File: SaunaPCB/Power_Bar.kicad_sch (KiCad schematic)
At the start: 58 parts, among them J201 KL3RM7.62, J202 KL3RM7.62, J203 KL3RM7.62, J204 KL2RM5.08, J205 KL3RM7.62, J206 KL3RM7.62, K201 RP310024, K202 RP310024, K203 RP310024, K204 RP310024, K205 RP310024, K206 RP310024, K207 RP310024, U201 LHE05-20B24, U202 LM2576T-5, U203 4N25, U204 4N25, U205 4N25, U206 DRV5053, U207 DRV5053, U208 DRV5053

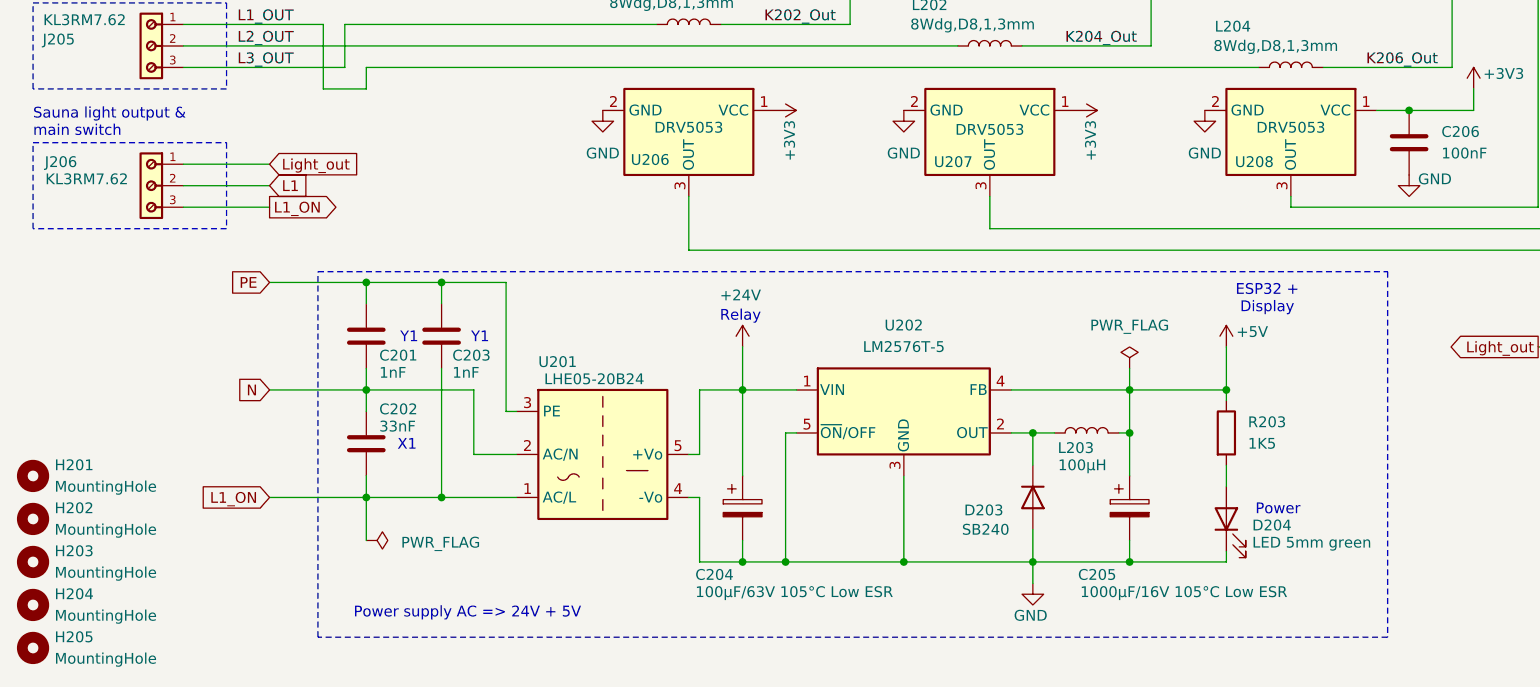
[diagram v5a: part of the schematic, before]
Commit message: ^MOV and Fuse added
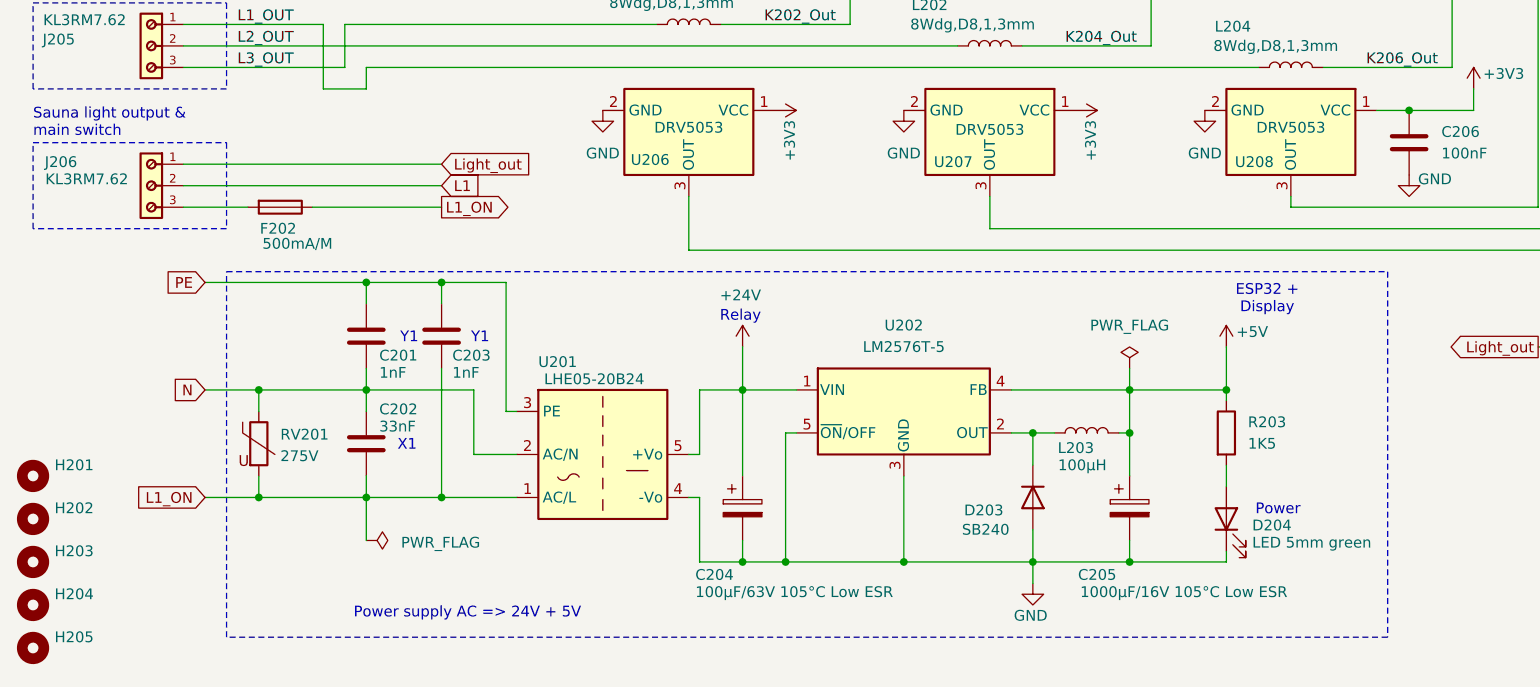
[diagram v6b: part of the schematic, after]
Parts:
- added F202: 500mA/M, Fuse:Fuseholder_Cylinder-5x20mm_Schurter_0031_8201_Horizontal_Open, symbol Device:Fuse
- added RV201: 275V, Varistor:RV_Disc_D12mm_W4.2mm_P7.5mm, symbol Device:Varistor
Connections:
- net L1_ON: now also F202.1, RV201.2; no longer J206.3
- net N: now also RV201.1
- new net: F202.2, J206.3

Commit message: Power LED changed to JST connector KTY room added
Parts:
- D204: footprint Connector_JST:JST_EH_B2B-EH-A_1x02_P2.50mm_Vertical -> MyConnectors:B2B-ZR
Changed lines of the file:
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@@
 			)
 		)
-		(property "Footprint" "Connector_JST:JST_EH_B2B-EH-A_1x02_P2.50mm_Vertical"
+		(property "Footprint" "MyConnectors:B2B-ZR"
 			(at 156.21 177.8 0)
 			(effects

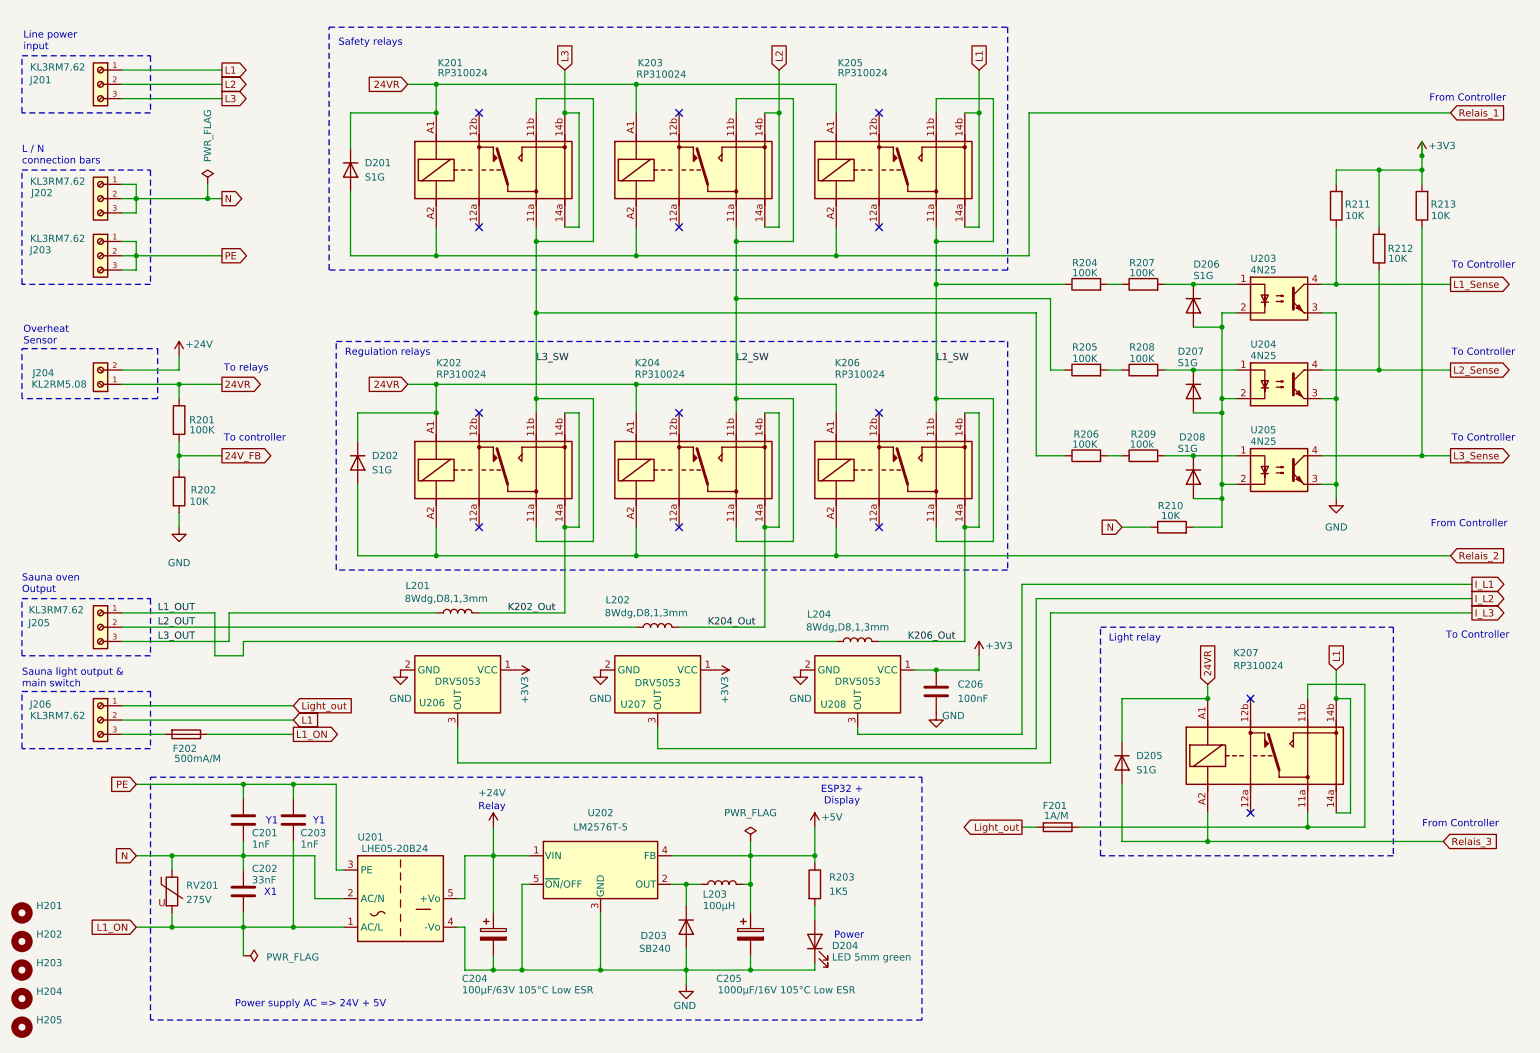
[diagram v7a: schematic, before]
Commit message: Home brew sensor: Coil and hall sensor combined to one unit to avoid overlap errors on DRC DRC errors removed; 2 warnings left => both acceptable.
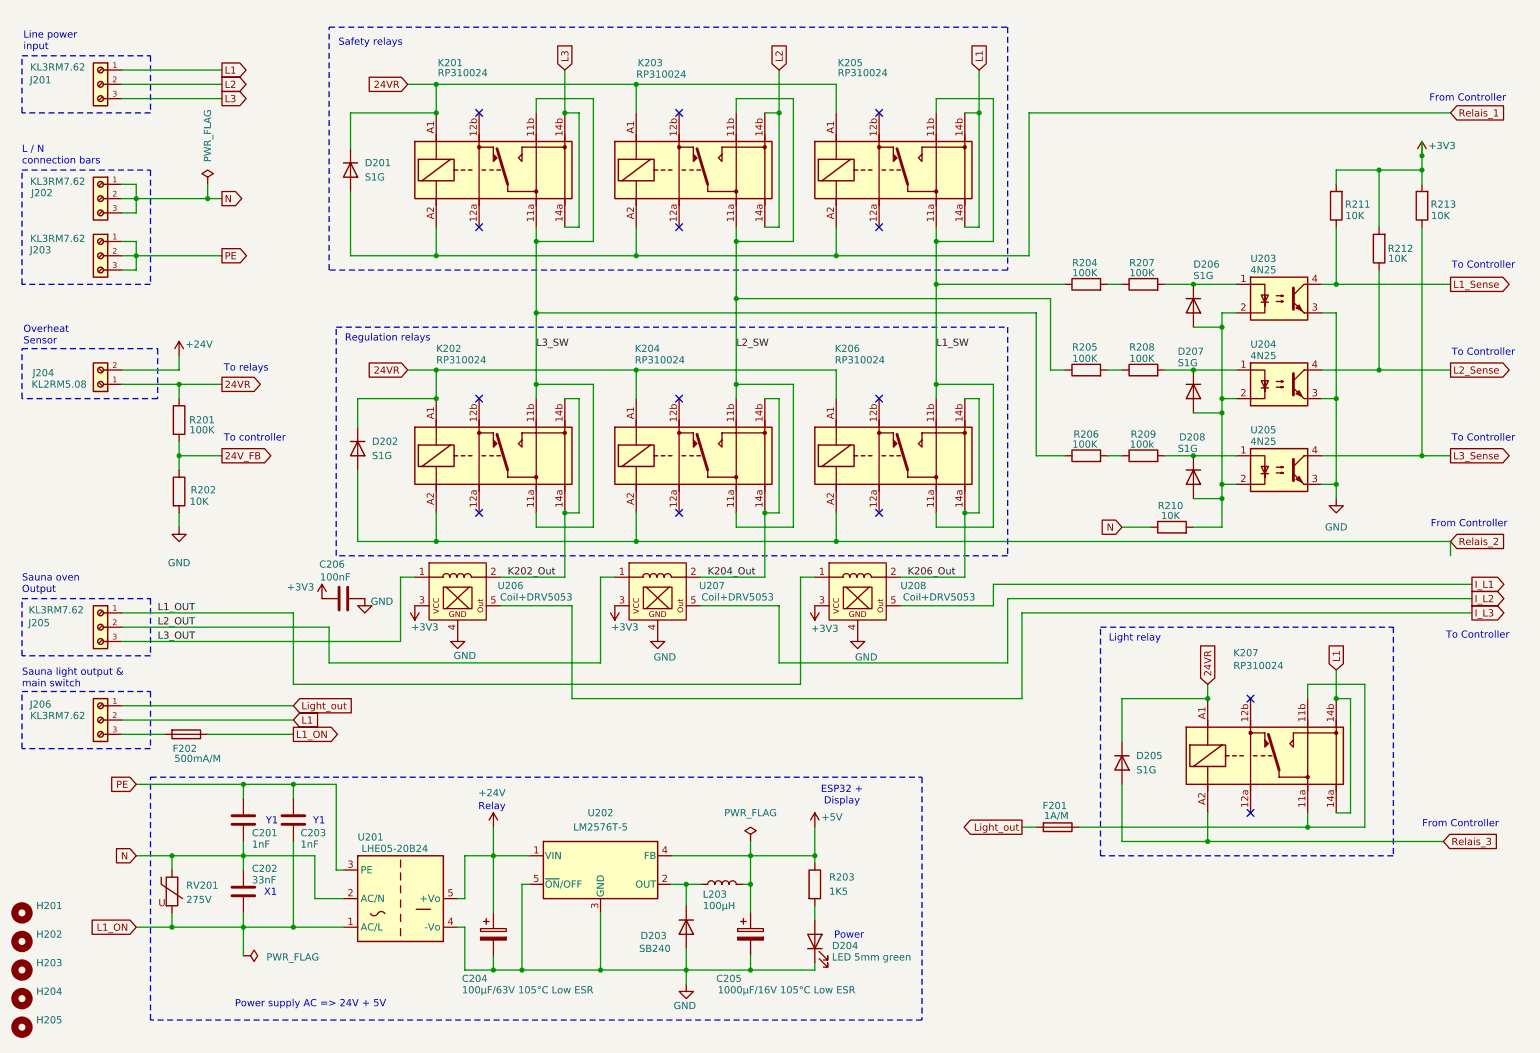
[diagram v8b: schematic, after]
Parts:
- removed L201, L202, L204: 8Wdg,D8,1,3mm, SaunaProject:Current_Coil_19X14, symbol Device:L
- removed U206, U207, U208: DRV5053, Package_TO_SOT_THT:TO-92_Inline, symbol Sensor_Magnetic:DRV5033AJxLPG
- added U206, U207, U208: Coil+DRV5053, SaunaProject:Current_Coil_19X14_w_Hall, symbol Project:HomeBrewISens
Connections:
- net +3V3: now also U206.3, U207.3, U208.3
- net GND: now also U206.4, U207.4, U208.4
- net I_L1: now also U208.5
- net I_L2: now also U207.5
- net I_L3: now also U206.5
- net K202_Out: now also U206.2
- net K204_Out: now also U207.2
- net K206_Out: now also U208.2
- net L1_OUT: now also U208.1
- net L2_OUT: now also U207.1
- net L3_OUT: now also U206.1
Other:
- moved on the sheet: C206, D202, K202, K204, K206
